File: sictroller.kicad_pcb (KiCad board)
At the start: 6 copper layers, 314 parts, among them J1 CONN_01X02, J10 CONN_01X02, J11 RINGTERM, J12 RINGTERM, J13 CONN_01X01, J2 CONN_01X08, J3 CONN_02X05, J4 RINGTERM, J5 RINGTERM, J6 RINGTERM, J7 CONN_01X02, J8 RINGTERM, J9 RINGTERM, P1 CONN_01X03, Q1 CSD17483F4, Q2 CCS050M12CM2, T1 7508110151, U1 ACPL-M61L, U10 74LVC2G04, U11 TXS0108E, U12 MGJ1, U13 MGJ1, U14 2ED020I12-F2, U15 MGJ1, U16 MGJ1, U17 2ED020I12-F2, U18 MGJ1, U19 MGJ1, U2 TMS320F28069M, U20 2ED020I12-F2, U3 ADM3053, U4 TPS76201, U5 TPS76201, U6 XCL221B18, U7 VIPER26HD, U8 ADUM5241, U9 MAX6691, Y1 CSTCE20M0V13C

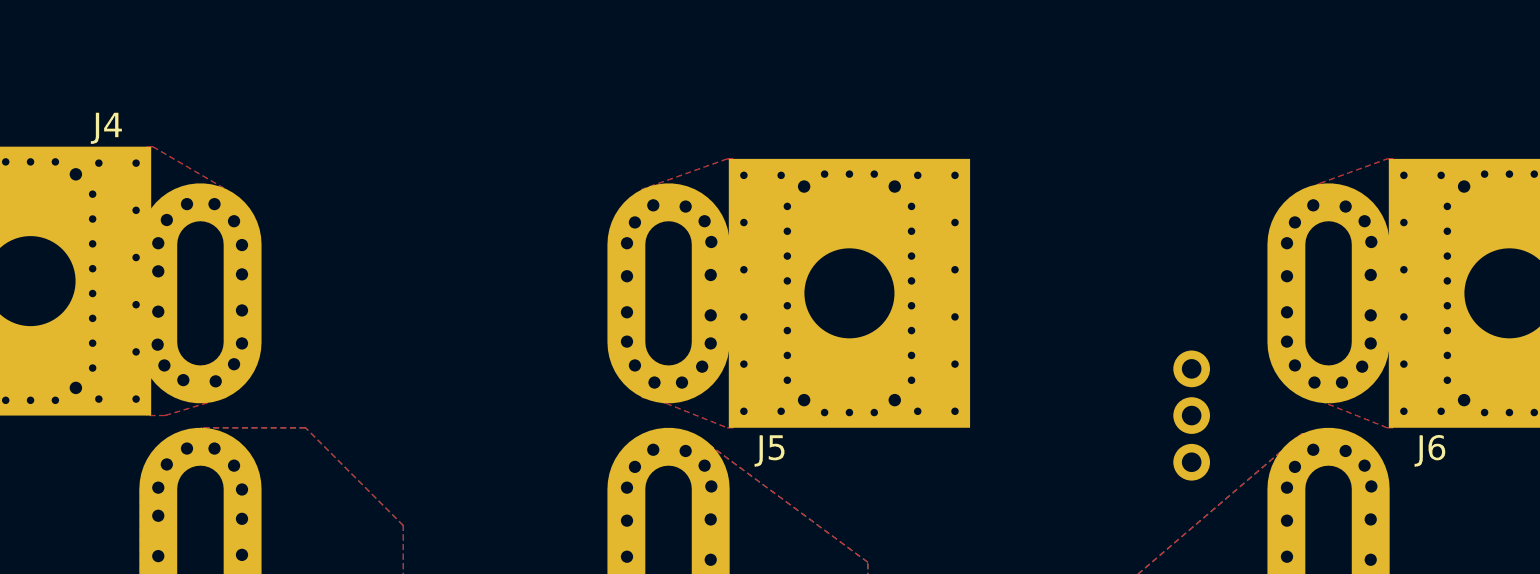
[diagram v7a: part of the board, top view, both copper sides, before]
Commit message: Zones for phase connections 3
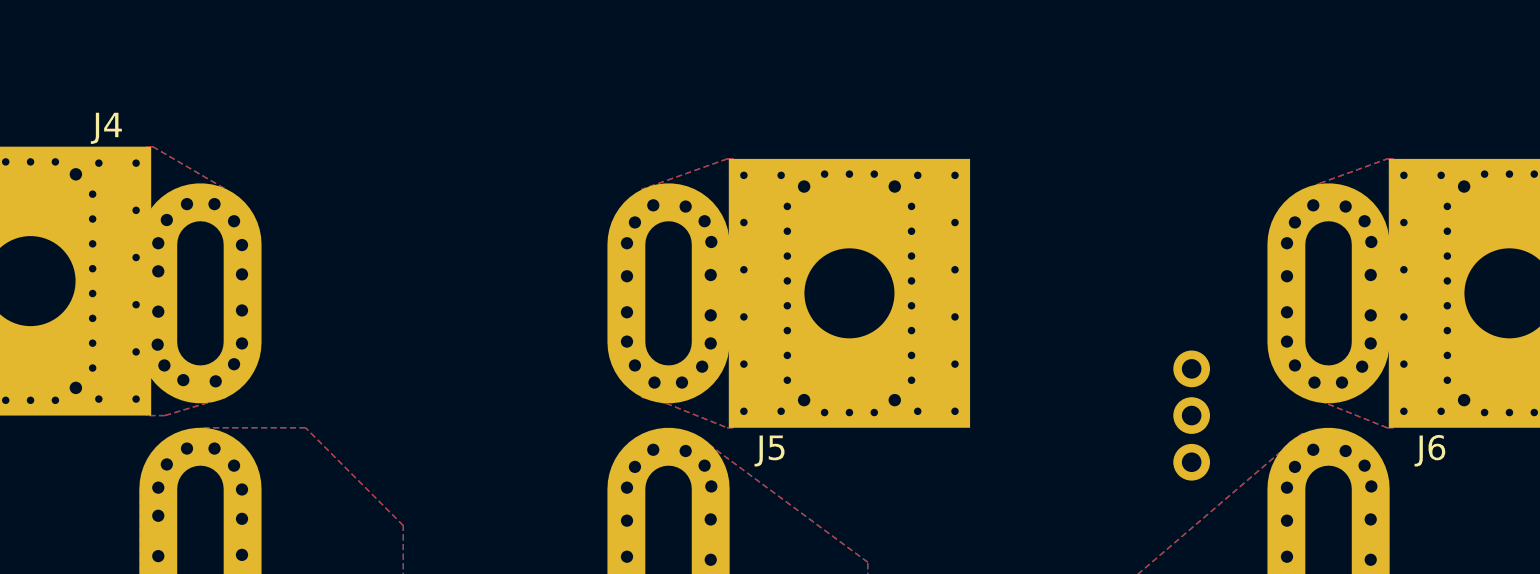
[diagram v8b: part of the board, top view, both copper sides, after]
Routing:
- added copper zone on B.Cu, net /Feedback/A
- added copper zone on In1.Cu, net /Feedback/A
- added copper zone on In2.Cu, net /Feedback/A
- added copper zone on In3.Cu, net /Feedback/A
- added copper zone on In4.Cu, net /Feedback/A
- added copper zone on B.Cu, net /Feedback/B
- added copper zone on In1.Cu, net /Feedback/B
- added copper zone on In2.Cu, net /Feedback/B
- added copper zone on In3.Cu, net /Feedback/B
- added copper zone on In4.Cu, net /Feedback/B
- added copper zone on B.Cu, net /Feedback/C
- added copper zone on In1.Cu, net /Feedback/C
- added copper zone on In2.Cu, net /Feedback/C
- added copper zone on In3.Cu, net /Feedback/C
- added copper zone on In4.Cu, net /Feedback/C
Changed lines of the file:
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@@
+    )
+  )
+  (zone (net 140) (net_name /Feedback/A) (layer B.Cu) (hatch edge 0.508)
+    (connect_pads yes (clearance 0.65))
+    (min_thickness 0.2032)
+    (fill yes (arc_segments 32) (thermal_gap 0.508) (thermal_bridge_width 0.508))
+    (polygon
+      (pts
+        (xy 75.5 28) (xy 78.5 29.75) (xy 78.5 38.25) (xy 76 39) (xy 75.25 39)
+        (xy 75.25 28)
+      )
+    )
+  )
+  (zone (net 140) (net_name /Feedback/A) (layer In1.Cu) (hatch edge 0.508)
+    (connect_pads yes (clearance 0.4))
+    (min_thickness 0.2032)
+    (fill yes (arc_segments 32) (thermal_gap 0.508) (thermal_bridge_width 0.508))
+    (polygon
+      (pts
+        (xy 75.5 28) (xy 78.5 29.75) (xy 78.5 38.25) (xy 76 39) (xy 75.25 39)
+        (xy 75.25 28)
+      )
+    )
+  )
+  (zone (net 140) (net_name /Feedback/A) (layer In2.Cu) (hatch edge 0.508)
+    (connect_pads yes (clearance 0.4))
+    (min_thickness 0.2032)
+    (fill yes (arc_segments 32) (thermal_gap 0.508) (thermal_bridge_width 0.508))
+    (polygon
+      (pts
+        (xy 75.5 28) (xy 78.5 29.75) (xy 78.5 38.25) (xy 76 39) (xy 75.25 39)
+        (xy 75.25 28)
+      )
+    )
+  )
+  (zone (net 140) (net_name /Feedback/A) (layer In3.Cu) (hatch edge 0.508)
+    (connect_pads yes (clearance 0.4))
+    (min_thickness 0.2032)
+    (fill yes (arc_segments 32) (thermal_gap 0.508) (thermal_bridge_width 0.508))
+    (polygon
+      (pts
+        (xy 75.5 28) (xy 78.5 29.75) (xy 78.5 38.25) (xy 76 39) (xy 75.25 39)
+        (xy 75.25 28)
+      )
+    )
+  )
+  (zone (net 140) (net_name /Feedback/A) (layer In4.Cu) (hatch edge 0.508)
+    (connect_pads yes (clearance 0.4))
+    (min_thickness 0.2032)
+    (fill yes (arc_segments 32) (thermal_gap 0.508) (thermal_bridge_width 0.508))
+    (polygon
+      (pts
+        (xy 75.5 28) (xy 78.5 29.75) (xy 78.5 38.25) (xy 76 39) (xy 75.25 39)
+        (xy 75.25 28)
+      )
     )
   )
@@
     )
   )
-  (zone (net 142) (net_name /Feedback/C) (layer F.Cu) (hatch edge 0.508)
-    (connect_pads yes (clearance 0.6))
+  (zone (net 141) (net_name /Feedback/B) (layer B.Cu) (hatch edge 0.508)
+    (connect_pads yes (clearance 0.65))
     (min_thickness 0.2032)
     (fill yes (arc_segments 32) (thermal_gap 0.508) (thermal_bridge_width 0.508))
+    (polygon
+      (pts
+        (xy 99.25 28.5) (xy 99 28.5) (xy 95.5 29.75) (xy 95.5 38.25) (xy 96.5 38.5)
+        (xy 99 39.5) (xy 99.25 39.5)
+      )
+    )
+  )
+  (zone (net 141) (net_name /Feedback/B) (layer In1.Cu) (hatch edge 0.508)
+    (connect_pads yes (clearance 0.4))
+    (min_thickness 0.2032)
+    (fill yes (arc_segments 32) (thermal_gap 0.508) (thermal_bridge_width 0.508))
+    (polygon
+      (pts
+        (xy 99.25 28.5) (xy 99 28.5) (xy 95.5 29.75) (xy 95.5 38.25) (xy 96.5 38.5)
+        (xy 99 39.5) (xy 99.25 39.5)
+      )
+    )
+  )
+  (zone (net 141) (net_name /Feedback/B) (layer In2.Cu) (hatch edge 0.508)
+    (connect_pads yes (clearance 0.4))
+    (min_thickness 0.2032)
+    (fill yes (arc_segments 32) (thermal_gap 0.508) (thermal_bridge_width 0.508))
+    (polygon
+      (pts
+        (xy 99.25 28.5) (xy 99 28.5) (xy 95.5 29.75) (xy 95.5 38.25) (xy 96.5 38.5)
+        (xy 99 39.5) (xy 99.25 39.5)
+      )
+    )
+  )
+  (zone (net 141) (net_name /Feedback/B) (layer In3.Cu) (hatch edge 0.508)
+    (connect_pads yes (clearance 0.4))
+    (min_thickness 0.2032)
+    (fill yes (arc_segments 32) (thermal_gap 0.508) (thermal_bridge_width 0.508))
+    (polygon
+      (pts
+        (xy 99.25 28.5) (xy 99 28.5) (xy 95.5 29.75) (xy 95.5 38.25) (xy 96.5 38.5)
+        (xy 99 39.5) (xy 99.25 39.5)
+      )
+    )
+  )
+  (zone (net 141) (net_name /Feedback/B) (layer In4.Cu) (hatch edge 0.508)
+    (connect_pads yes (clearance 0.4))
+    (min_thickness 0.2032)
+    (fill yes (arc_segments 32) (thermal_gap 0.508) (thermal_bridge_width 0.508))
+    (polygon
+      (pts
+        (xy 99.25 28.5) (xy 99 28.5) (xy 95.5 29.75) (xy 95.5 38.25) (xy 96.5 38.5)
+        (xy 99 39.5) (xy 99.25 39.5)
+      )
+    )
+  )
+  (zone (net 142) (net_name /Feedback/C) (layer F.Cu) (hatch edge 0.508)
+    (connect_pads yes (clearance 0.65))
+    (min_thickness 0.2032)
+    (fill yes (arc_segments 32) (thermal_gap 0.508) (thermal_bridge_width 0.508))
+    (polygon
+      (pts
+        (xy 123.5 38.5) (xy 122.75 38) (xy 122.75 29.75) (xy 123.25 29.5) (xy 126 28.5)
+        (xy 126.25 28.5) (xy 126.25 39.5) (xy 126 39.5)
+      )
+    )
+  )
+  (zone (net 142) (net_name /Feedback/C) (layer B.Cu) (hatch edge 0.508)
+    (connect_pads yes (clearance 0.65))
+    (min_thickness 0.2032)
+    (fill yes (arc_segments 32) (thermal_gap 0.508) (thermal_bridge_width 0.508))
+    (polygon
+      (pts
+        (xy 123.5 38.5) (xy 122.75 38) (xy 122.75 29.75) (xy 123.25 29.5) (xy 126 28.5)
+        (xy 126.25 28.5) (xy 126.25 39.5) (xy 126 39.5)
+      )
+    )
+  )
+  (zone (net 142) (net_name /Feedback/C) (layer In1.Cu) (hatch edge 0.508)
+    (connect_pads yes (clearance 0.4))
+    (min_thickness 0.2032)
+    (fill yes (arc_segments 32) (thermal_gap 0.508) (thermal_bridge_width 0.508))
+    (polygon
+      (pts
+        (xy 123.5 38.5) (xy 122.75 38) (xy 122.75 29.75) (xy 123.25 29.5) (xy 126 28.5)
+        (xy 126.25 28.5) (xy 126.25 39.5) (xy 126 39.5)
+      )
+    )
+  )
+  (zone (net 142) (net_name /Feedback/C) (layer In2.Cu) (hatch edge 0.508)
+    (connect_pads yes (clearance 0.4))
+    (min_thickness 0.2032)
+    (fill yes (arc_segments 32) (thermal_gap 0.508) (thermal_bridge_width 0.508))
+    (polygon
+      (pts
+        (xy 123.5 38.5) (xy 122.75 38) (xy 122.75 29.75) (xy 123.25 29.5) (xy 126 28.5)
+        (xy 126.25 28.5) (xy 126.25 39.5) (xy 126 39.5)
+      )
+    )
+  )
+  (zone (net 142) (net_name /Feedback/C) (layer In3.Cu) (hatch edge 0.508)
+    (connect_pads yes (clearance 0.4))
+    (min_thickness 0.2032)
+    (fill yes (arc_segments 32) (thermal_gap 0.508) (thermal_bridge_width 0.508))
+    (polygon
+      (pts
+        (xy 123.5 38.5) (xy 122.75 38) (xy 122.75 29.75) (xy 123.25 29.5) (xy 126 28.5)
+        (xy 126.25 28.5) (xy 126.25 39.5) (xy 126 39.5)
+      )
+    )
+  )
+  (zone (net 142) (net_name /Feedback/C) (layer In4.Cu) (hatch edge 0.508)
+    (connect_pads yes (clearance 0.4))
+    (min_thickness 0.2032)
+    (fill yes (arc_segments 32) (thermal_gap 0.508) (thermal_bridge_width 0.508))
